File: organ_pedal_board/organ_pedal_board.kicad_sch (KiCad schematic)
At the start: 6 parts, among them J1 Conn_01x15_Socket, J2 Conn_01x15_Socket, U1 LM358

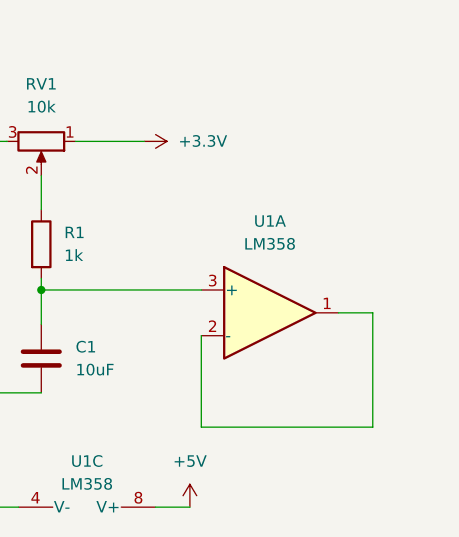
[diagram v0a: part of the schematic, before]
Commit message: Add resistor R2 to the schematic at (171.45, 106.68)
- Introduced a new resistor component (R2) with a value of 100 ohms.
- Added a junction point to connect the resistor within the circuit.
- Updated properties for the resistor including reference, value, and datasheet.
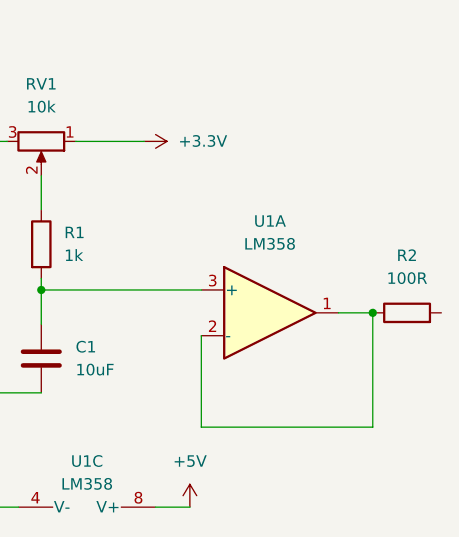
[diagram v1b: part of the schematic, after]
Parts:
- added R2: 100R, symbol Device:R
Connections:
- net at U1.1, U1.2 (-): now also R2.1
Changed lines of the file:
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@@
   (junction (at 116.84 115.57) (diameter 0) (color 0 0 0 0)
+  )
+  (junction (at 167.64 106.68) (diameter 0) (color 0 0 0 0)
   )
   (wire (pts (xy 167.64 119.38) (xy 167.64 106.68))
@@
         )
       )
+    )
+  )
+  (symbol (lib_id "Device:R") (at 171.45 106.68 90) (unit 1)
+    (in_bom yes) (on_board yes) (dnp no) (fields_autoplaced)
+    (property "Reference" "R2" (at 171.45 100.33 90)
+      (effects (font (size 1.27 1.27)))
+    )
+    (property "Value" "100R" (at 171.45 102.87 90)
+      (effects (font (size 1.27 1.27)))
+    )
+    (property "Footprint" "" (at 171.45 108.458 90)
+      (effects (font (size 1.27 1.27)) hide)
+    )
+    (property "Datasheet" "~" (at 171.45 106.68 0)
+      (effects (font (size 1.27 1.27)) hide)
+    )
+    (pin "2")
+    (pin "1")
+    (instances
+      (project "organ_pedal_board"
+        (path "/2fa41924-6213-48e9-b230-05fde6975ac3"
+          (reference "R2") (unit 1)
+        )
+      )

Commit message: Refactor code structure for improved readability and maintainability
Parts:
- removed J1, J2: Conn_01x15_Socket, symbol Connector:Conn_01x15_Socket
- removed RV1: 10k, symbol Device:R_Potentiometer
- removed U1: LM358, symbol Amplifier_Operational:LM358
- added C2: 10uF, symbol Device:C
- added C3, C4: 1uF, symbol Device:C
- added C5: 100nF, symbol Device:C
- added J1: AudioPlug3, symbol Connector_Audio:AudioPlug3
- added JP1: EN, symbol Jumper:SolderJumper_2_Open
- added U1: LMV358, symbol Amplifier_Operational:LMV358
- added U2: ~, symbol esp32Node:esp32devkitv1
- added U3: ADS1115IDGS, Package_SO:TSSOP-10_3x3mm_P0.5mm, symbol Analog_ADC:ADS1115IDGS
- added U4: AP2112K-3.3, Package_TO_SOT_SMD:SOT-23-5, symbol Regulator_Linear:AP2112K-3.3
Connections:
- net +3.3V: now also C2.1, C3.1, C4.2, C5.1, J1.R, U1.8 (V+), U2.30 (VIN), U3.8 (VDD), U4.5 (VOUT)
- net GND: now also C4.1, C5.2, J1.S, U1.4 (V-), U2.2 (GND), U2.29 (GND), U3.1 (ADDR), U3.3 (GND)
- net pedal_out: now reaches R1.1
- net pedal_out: now also J1.T
- net at R2.1: now also U1.1, U1.2 (-)
- net pedal_signal: now reaches R2.2
- net pedal_signal: now also U3.4 (AIN0)
- net at C1.1, R1.2: now also U1.3 (+)
- new net: C2.2, C3.2, U4.2 (GND)
- new net: JP1.2 (B), U4.3 (EN)
- new net 5v: JP1.1 (A), U4.1 (VIN)
- new net dready: U2.15 (D23), U3.2 (ALERT/RDY)
- new net i2c_scl: U2.14 (D22), U3.10 (SCL)
- new net i2c_sda: U2.11 (D21), U3.9 (SDA)
- no-connect marks 0 -> 24
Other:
- moved on the sheet: C1, R1, R2

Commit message: Implement feature X to enhance user experience and fix bug Y in module Z
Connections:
- net GND: now also C2.2, C3.2, U4.2 (GND)
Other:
- moved on the sheet: C1, C4, C5, J1, R1, R2, U1A, U1C, U3

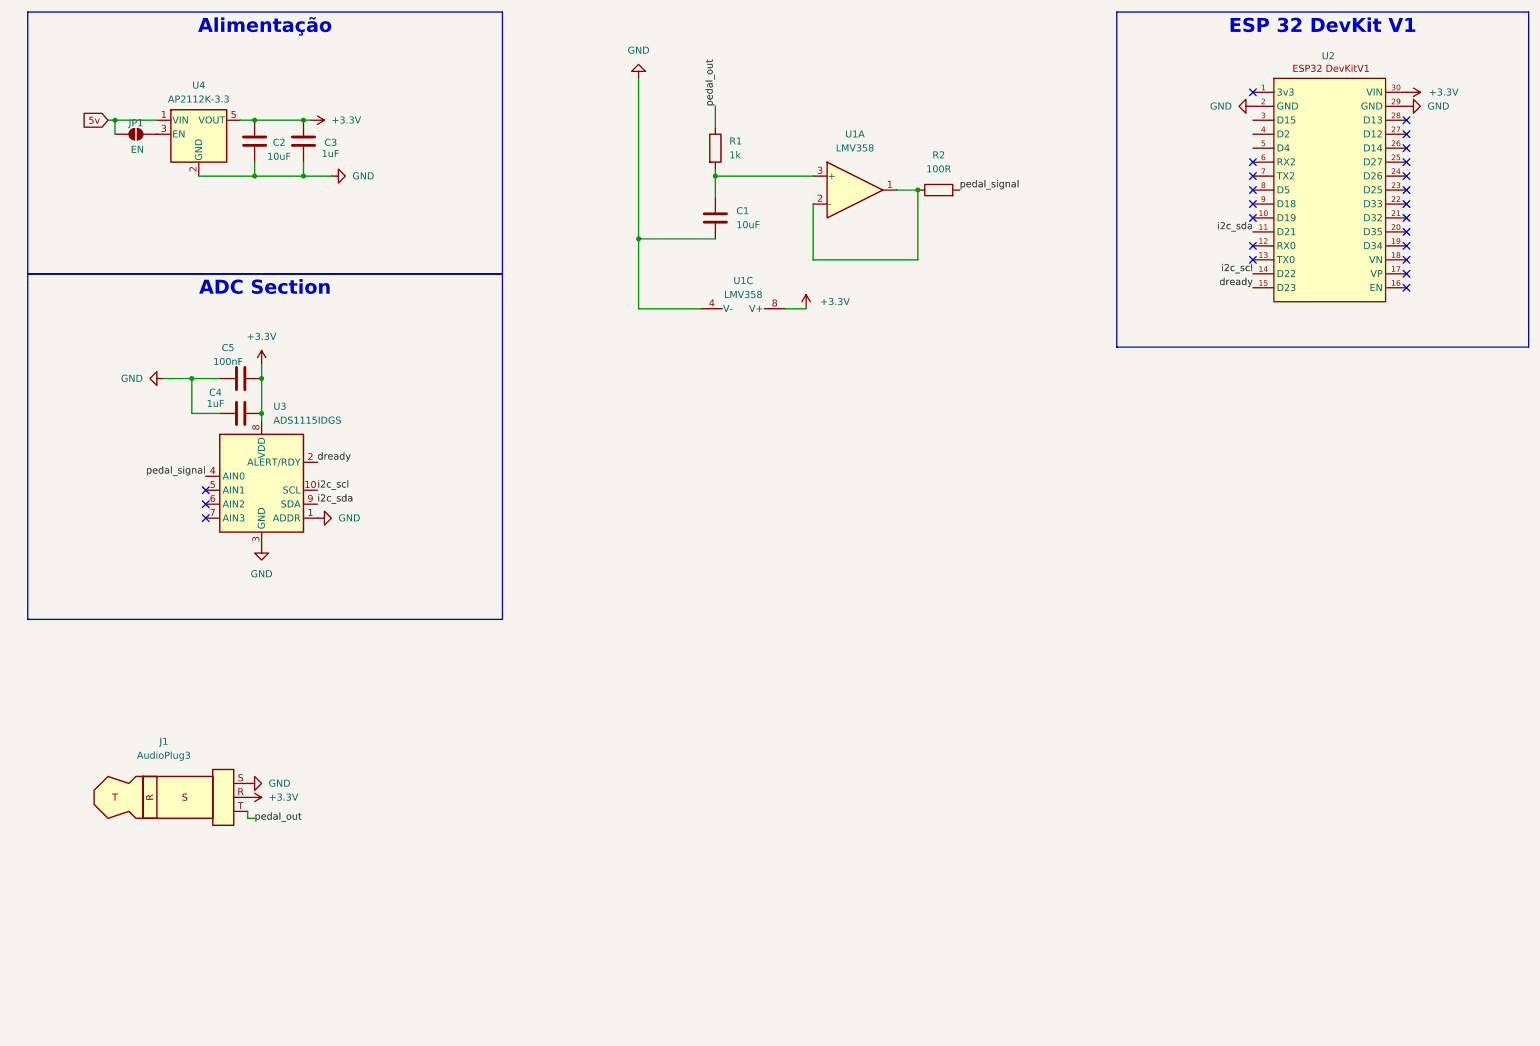
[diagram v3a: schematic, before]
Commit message: Add text annotations and adjust component positions in schematic
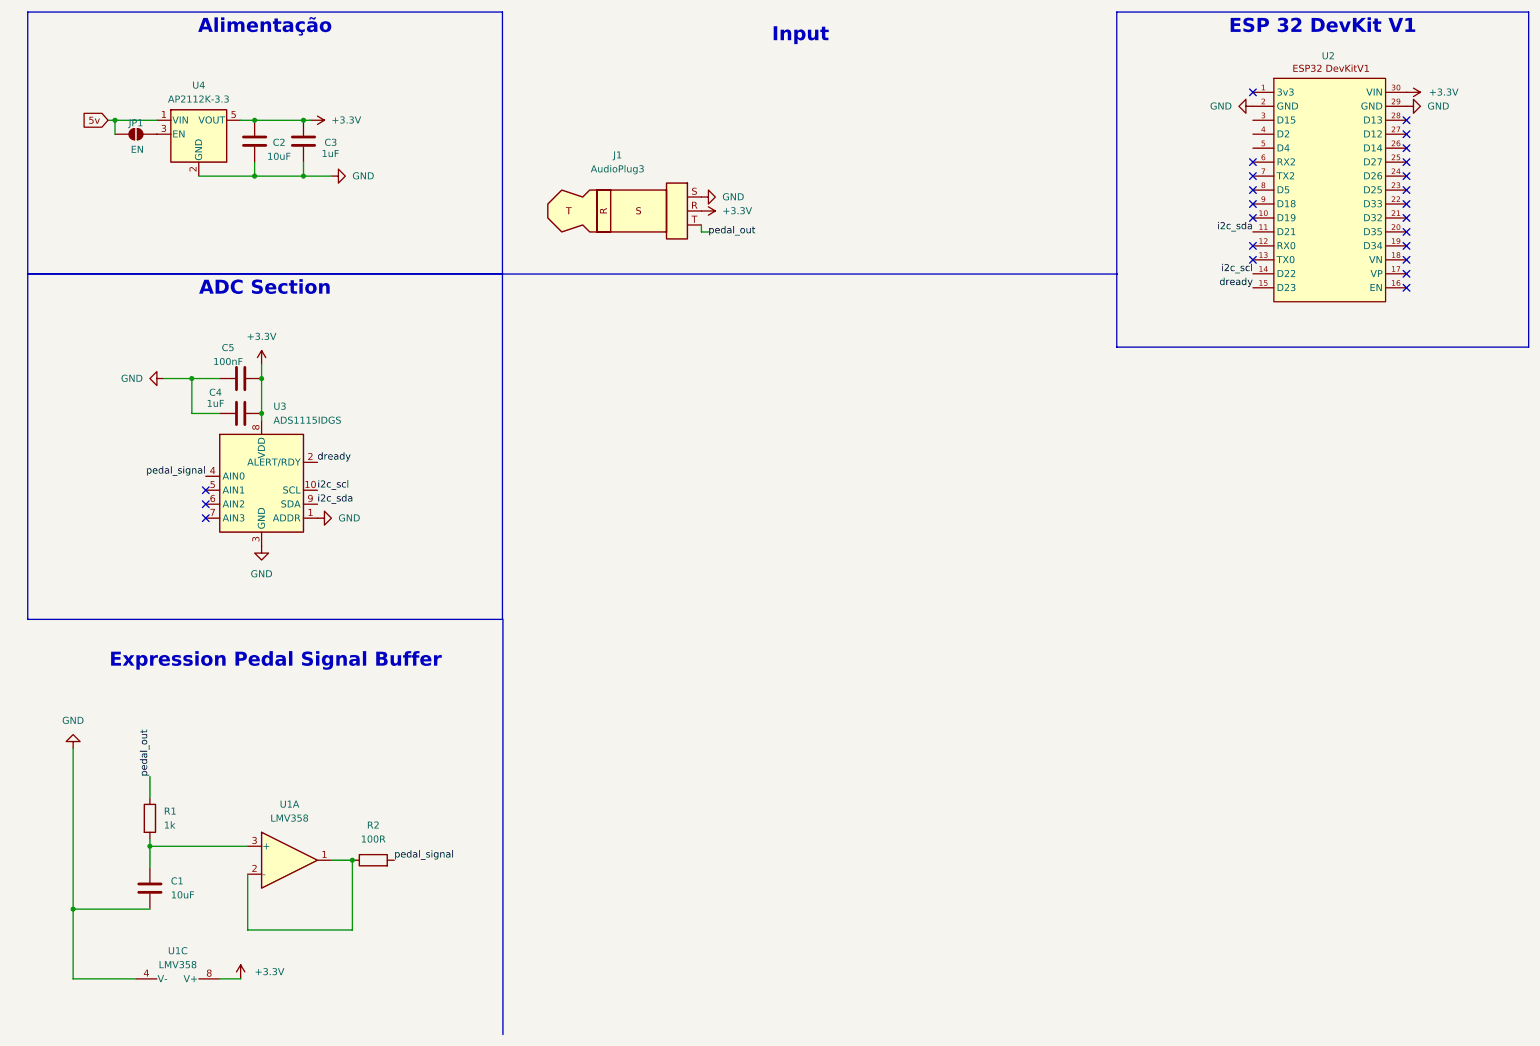
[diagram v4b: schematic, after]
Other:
- note added: "Expression Pedal Signal Buffer"
- note added: "Input"
- moved on the sheet: C1, J1, R1, R2, U1A, U1C

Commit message: Feat
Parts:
- removed U1: LMV358, symbol Amplifier_Operational:LMV358
- added C6: 10uF, symbol Device:C
- added C7, C8: 200pF, symbol Device:C
- added J2: AudioPlug3, symbol Connector_Audio:AudioPlug3
- added R3: 1, symbol Device:R
- added R4: 100R, symbol Device:R
- added U1: MCP6002-xSN, Package_SO:SOIC-8_3.9x4.9mm_P1.27mm, symbol Amplifier_Operational:MCP6002-xSN
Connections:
- net +3.3V: now also J2.R, U1.4 (V-)
- net GND: now also C6.2, C7.2, C8.2, J2.S, U1.8 (V+)
- net at R2.1: now also U1.1, U1.2 (-)
- net pedal2_signal: now reaches U3.5 (AIN1)
- net pedal2_signal: now also C8.1, R4.2
- net at C1.1, R1.2: now also U1.3 (+)
- net pedal_out renamed pedal1_out
- net pedal_signal renamed pedal1_signal
- net pedal1_signal: now also C7.1
- new net: C6.1, R3.2, U1.5 (+)
- new net: R4.1, U1.6 (-), U1.7
- new net pedal2_out: J2.T, R3.1
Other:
- note added: "Pedals Signal Buffer"
- note removed: "Expression Pedal Signal Buffer"
- moved on the sheet: C1, J1, R1, R2
